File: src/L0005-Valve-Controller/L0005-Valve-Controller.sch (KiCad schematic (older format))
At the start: 24 parts, among them P1 3220-20-0200-00, U1 LPC54113J256BD64QL, U2 LMS8117AMP-3.3_NOPB

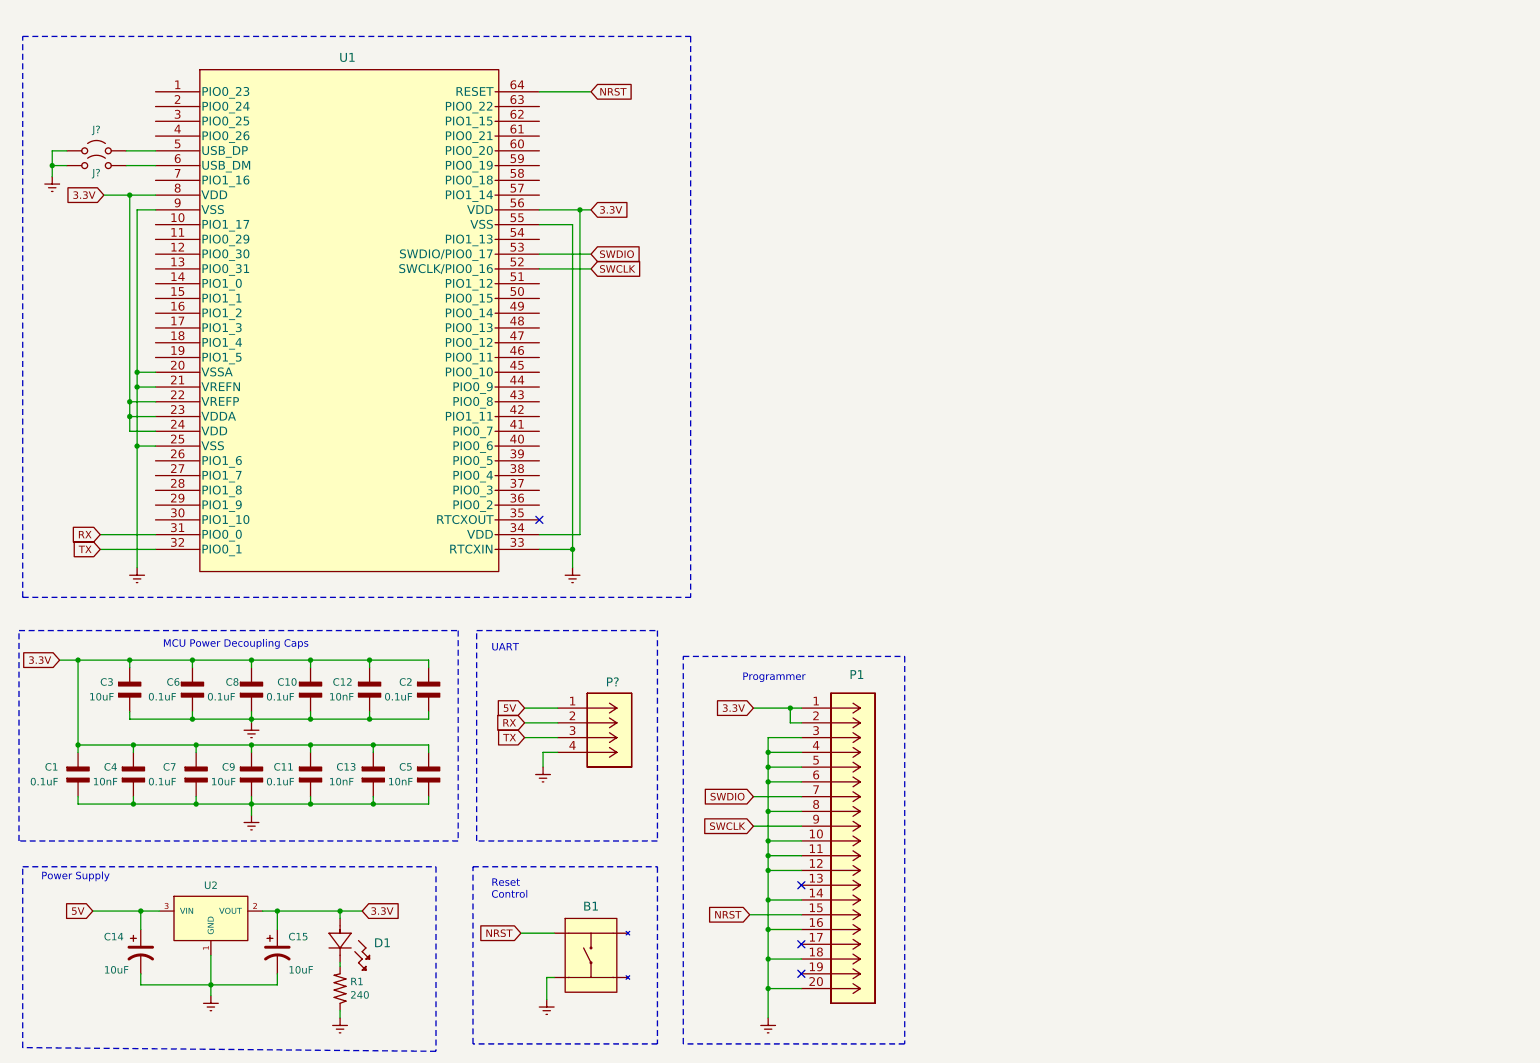
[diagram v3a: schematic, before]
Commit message: Added SSR Solenoid drivers to schematic
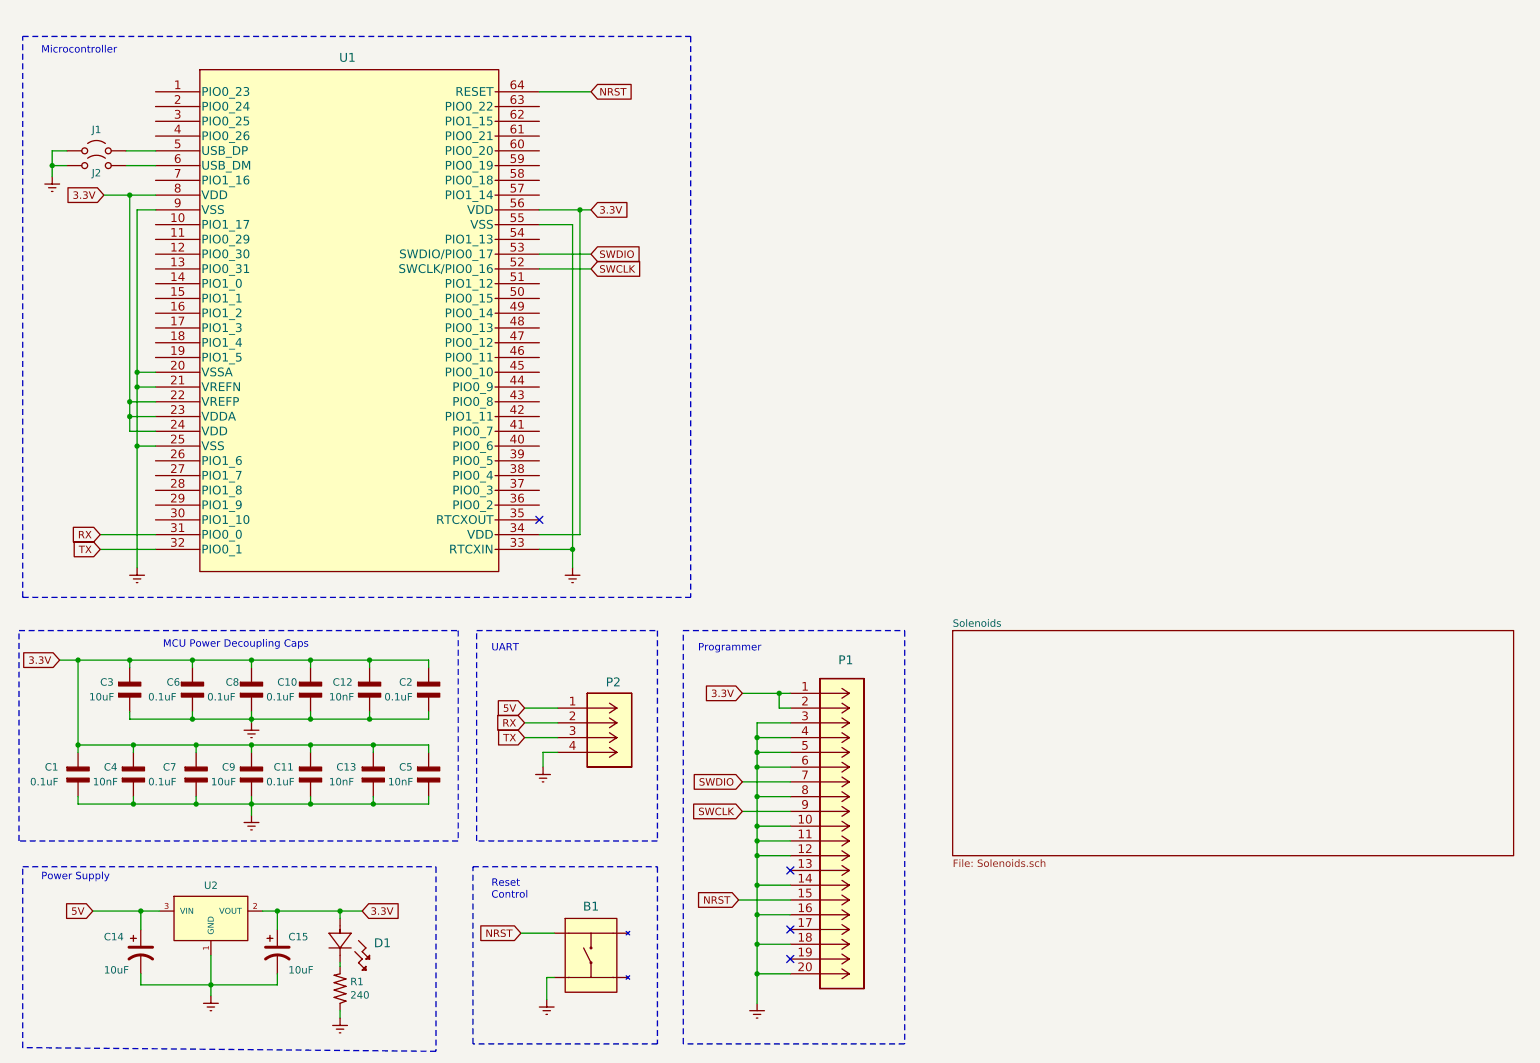
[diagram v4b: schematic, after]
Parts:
- gave numbers to parts that had none: 3
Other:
- note added: "Microcontroller"
- moved on the sheet: P1
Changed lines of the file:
@@
 $Descr A4 11693 8268
 encoding utf-8
-Sheet 1 1
+Sheet 1 2
 Title "L0005 Valve Controller"
 Date "2021-12-25"
@@
 $EndComp
 NoConn ~ 4300 4025
-Text Notes 5675 5125 0    50   ~ 0
+Text Notes 5375 4925 0    50   ~ 0
 Programmer
 $Comp
 L L0005-Valve-Controller:3220-20-0200-00 P1
 U 1 1 61D6852B
-P 6075 5300
-F 0 "P1" H 6400 5525 60  0000 L CNN
-F 1 "3220-20-0200-00" H 6475 5450 60  0001 C CNN
-F 2 "CONN20_D10-RA-BK_SUL" H 6475 4240 60  0001 C CNN
-F 3 "" H 6075 5300 60  0001 C CNN
-	1    6075 5300
-	1    0    0    -1
-$EndComp
-Text GLabel 5750 5300 0    50   Input ~ 0
+P 6000 5200
+F 0 "P1" H 6325 5425 60  0000 L CNN
+F 1 "3220-20-0200-00" H 6400 5350 60  0001 C CNN
+F 2 "CONN20_D10-RA-BK_SUL" H 6400 4140 60  0001 C CNN
+F 3 "" H 6000 5200 60  0001 C CNN
+	1    6000 5200
+	1    0    0    -1
+$EndComp
+Text GLabel 5675 5200 0    50   Input ~ 0
 3.3V
 Wire Wire Line
-	5750 5300 6000 5300
-Wire Wire Line
-	6075 5400 6000 5400
-Wire Wire Line
-	6000 5400 6000 5300
-Connection ~ 6000 5300
-Wire Wire Line
-	6000 5300 6075 5300
+	5675 5200 5925 5200
+Wire Wire Line
+	6000 5300 5925 5300
+Wire Wire Line
+	5925 5300 5925 5200
+Connection ~ 5925 5200
+Wire Wire Line
+	5925 5200 6000 5200
 $Comp
 L L0005-Valve-Controller:Earth #PWR08
 U 1 1 61D80BAC
-P 5850 7400
-F 0 "#PWR08" H 5850 7150 50  0001 C CNN
-F 1 "Earth" H 5850 7250 50  0001 C CNN
-F 2 "" H 5850 7400 50  0001 C CNN
-F 3 "" H 5850 7400 50  0001 C CNN
-	1    5850 7400
-	1    0    0    -1
-$EndComp
-Wire Wire Line
-	6075 5500 5850 5500
-Wire Wire Line
-	5850 5500 5850 5600
-Wire Wire Line
-	6075 5600 5850 5600
-Connection ~ 5850 5600
-Wire Wire Line
-	5850 5600 5850 5700
-Wire Wire Line
-	6075 5700 5850 5700
-Connection ~ 5850 5700
-Wire Wire Line
-	5850 5700 5850 5800
-Wire Wire Line
-	6075 5800 5850 5800
-Connection ~ 5850 5800
-Wire Wire Line
-	5850 5800 5850 6000
-Text GLabel 5750 5900 0    50   Input ~ 0
+P 5775 7300
+F 0 "#PWR08" H 5775 7050 50  0001 C CNN
+F 1 "Earth" H 5775 7150 50  0001 C CNN
+F 2 "" H 5775 7300 50  0001 C CNN
+F 3 "" H 5775 7300 50  0001 C CNN
+	1    5775 7300
+	1    0    0    -1
+$EndComp
+Wire Wire Line
+	6000 5400 5775 5400
+Wire Wire Line
+	5775 5400 5775 5500
+Wire Wire Line
+	6000 5500 5775 5500
+Connection ~ 5775 5500
+Wire Wire Line
+	5775 5500 5775 5600
+Wire Wire Line
+	6000 5600 5775 5600
+Connection ~ 5775 5600
+Wire Wire Line
+	5775 5600 5775 5700
+Wire Wire Line
+	6000 5700 5775 5700
+Connection ~ 5775 5700
+Wire Wire Line
+	5775 5700 5775 5900
+Text GLabel 5675 5800 0    50   Input ~ 0
 SWDIO
 Wire Wire Line
-	6075 5900 5750 5900
-Text GLabel 5750 6100 0    50   Input ~ 0
+	6000 5800 5675 5800
+Text GLabel 5675 6000 0    50   Input ~ 0
 SWCLK
 Wire Wire Line
-	6075 6100 5750 6100
-Wire Wire Line
-	6075 6000 5850 6000
-Connection ~ 5850 6000
-Wire Wire Line
-	5850 6000 5850 6200
-Wire Wire Line
-	6075 6200 5850 6200
-Connection ~ 5850 6200
-Wire Wire Line
-	6075 6400 5850 6400
-Connection ~ 5850 6400
-Wire Wire Line
-	5850 6200 5850 6300
-Wire Wire Line
-	5850 6400 5850 6600
-Wire Wire Line
-	6075 6600 5850 6600
-Connection ~ 5850 6600
-Wire Wire Line
-	5850 6600 5850 6800
-Wire Wire Line
-	6075 6800 5850 6800
-Connection ~ 5850 6800
-Wire Wire Line
-	5850 6800 5850 7000
-Wire Wire Line
-	6075 7000 5850 7000
-Connection ~ 5850 7000
-Wire Wire Line
-	5850 7000 5850 7200
-Wire Wire Line
-	6075 7200 5850 7200
-Connection ~ 5850 7200
-Wire Wire Line
-	5850 7200 5850 7400
-Text GLabel 5725 6700 0    50   Input ~ 0
+	6000 6000 5675 6000
+Wire Wire Line
+	6000 5900 5775 5900
+Connection ~ 5775 5900
+Wire Wire Line
+	5775 5900 5775 6100
+Wire Wire Line
+	6000 6100 5775 6100
+Connection ~ 5775 6100
+Wire Wire Line
+	6000 6300 5775 6300
+Connection ~ 5775 6300
+Wire Wire Line
+	5775 6100 5775 6200
+Wire Wire Line
+	5775 6300 5775 6500
+Wire Wire Line
+	6000 6500 5775 6500
+Connection ~ 5775 6500
+Wire Wire Line
+	5775 6500 5775 6700
+Wire Wire Line
+	6000 6700 5775 6700
+Connection ~ 5775 6700
+Wire Wire Line
+	5775 6700 5775 6900
+Wire Wire Line
+	6000 6900 5775 6900
+Connection ~ 5775 6900
+Wire Wire Line
+	5775 6900 5775 7100
+Wire Wire Line
+	6000 7100 5775 7100
+Connection ~ 5775 7100
+Wire Wire Line
+	5775 7100 5775 7300
+Text GLabel 5650 6600 0    50   Input ~ 0
 NRST
 Wire Wire Line
-	5725 6700 6075 6700
-Wire Wire Line
-	6075 6300 5850 6300
-Connection ~ 5850 6300
-Wire Wire Line
-	5850 6300 5850 6400
-NoConn ~ 6075 6500
-NoConn ~ 6075 7100
-NoConn ~ 6075 6900
+	5650 6600 6000 6600
+Wire Wire Line
+	6000 6200 5775 6200
+Connection ~ 5775 6200
+Wire Wire Line
+	5775 6200 5775 6300
+NoConn ~ 6000 6400
+NoConn ~ 6000 7000
+NoConn ~ 6000 6800
 Text GLabel 4650 2225 2    50   Input ~ 0
 SWDIO
@@
 	4650 2325 4300 2325
 Wire Notes Line
-	5275 4950 6775 4950
-Wire Notes Line
-	6775 4950 6775 7575
+	5275 4775 6775 4775
+Wire Notes Line
+	6775 4775 6775 7575
 Wire Notes Line
 	6775 7575 5275 7575
 Wire Notes Line
-	5275 7575 5275 4950
+	5275 7575 5275 4775
 Wire Notes Line
 	3750 6200 775  6200
@@
 Reset \nControl
 $Comp
-L L0005-Valve-Controller:Jumper_NO J?
+L L0005-Valve-Controller:Jumper_NO J1
 U 1 1 620B41A7
 P 1300 1525
-F 0 "J?" H 1300 1668 50  0000 C CNN
+F 0 "J1" H 1300 1668 50  0000 C CNN
 F 1 "Jumper_NO" H 1300 1435 50  0001 C CNN
 F 2 "" H 1300 1525 50  0001 C CNN
@@
 $EndComp
 $Comp
-L L0005-Valve-Controller:Jumper_NO J?
+L L0005-Valve-Controller:Jumper_NO J2
 U 1 1 620C12B9
 P 1300 1625
-F 0 "J?" H 1300 1575 50  0000 C CNN
+F 0 "J2" H 1300 1575 50  0000 C CNN
 F 1 "Jumper_NO" H 1300 1535 50  0001 C CNN
 F 2 "" H 1300 1625 50  0001 C CNN
@@
 	1500 1625 1700 1625
 $Comp
-L L0005-Valve-Controller:Earth #PWR?
+L L0005-Valve-Controller:Earth #PWR09
 U 1 1 620CE508
 P 1000 1700
-F 0 "#PWR?" H 1000 1450 50  0001 C CNN
+F 0 "#PWR09" H 1000 1450 50  0001 C CNN
 F 1 "Earth" H 1000 1550 50  0001 C CNN
 F 2 "" H 1000 1700 50  0001 C CNN
@@
 	775  4775 3750 4775
 $Comp
-L L0005-Valve-Controller:140-504-415-000 P?
+L L0005-Valve-Controller:140-504-415-000 P2
 U 1 1 622DBA6B
 P 4425 5300
-F 0 "P?" H 4750 5475 60  0000 L CNN
+F 0 "P2" H 4750 5475 60  0000 L CNN
 F 1 "140-504-415-000" H 4775 4850 60  0001 C CNN
 F 2 "CONN_4840.2201_SCH" H 4825 4700 60  0001 C CNN
@@
 	4200 5300 4425 5300
 $Comp
-L L0005-Valve-Controller:Earth #PWR?
+L L0005-Valve-Controller:Earth #PWR010
 U 1 1 622F0D80
 P 4325 5700
-F 0 "#PWR?" H 4325 5450 50  0001 C CNN
+F 0 "#PWR010" H 4325 5450 50  0001 C CNN
 F 1 "Earth" H 4325 5550 50  0001 C CNN
 F 2 "" H 4325 5700 50  0001 C CNN
@@
 Wire Wire Line
 	1700 4225 1325 4225
+Text Notes 925  875  0    50   ~ 0
+Microcontroller
+$Sheet
+S 7100 4775 3800 1525
+U 624AA92C
+F0 "Solenoids" 50
+F1 "Solenoids.sch" 50
+$EndSheet
 $EndSCHEMATC

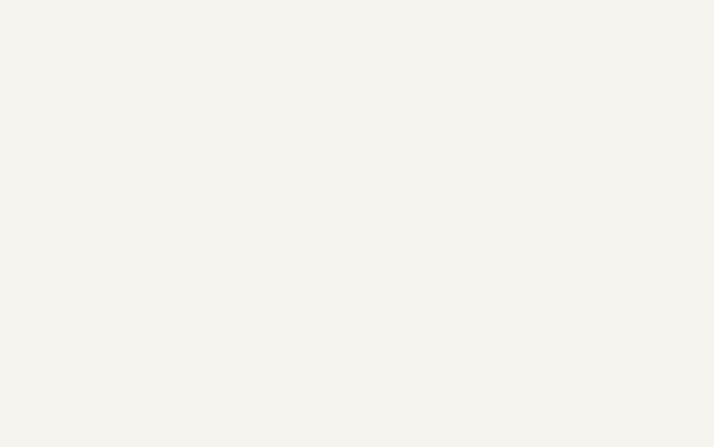
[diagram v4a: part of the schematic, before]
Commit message: Added AC source to schematic
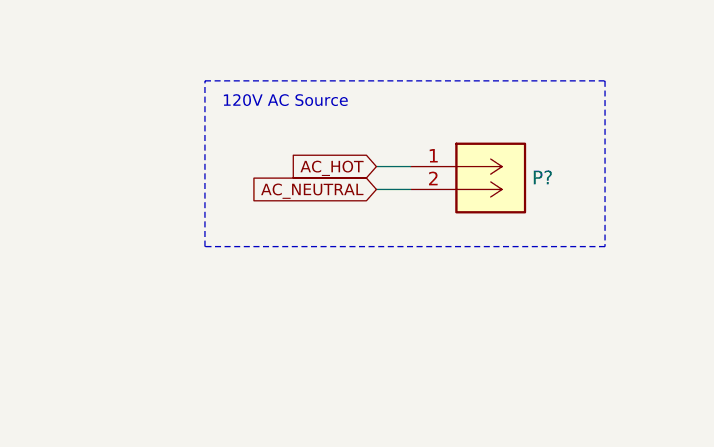
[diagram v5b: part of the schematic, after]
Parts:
- added P?: 647676-2, CONN_2043-1X04G00DAU_OUP, symbol L0005-Valve-Controller:647676-2
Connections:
- new net AC_HOT: P?.1
- new net AC_NEUTRAL: P?.2
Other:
- note added: "120V AC Source"
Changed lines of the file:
@@
 F1 "Solenoids.sch" 50
 $EndSheet
+$Comp
+L L0005-Valve-Controller:647676-2 P?
+U 1 1 62660979
+P 9650 1400
+F 0 "P?" H 10180 1350 60  0000 L CNN
+F 1 "647676-2" H 10178 1297 60  0001 L CNN
+F 2 "CONN_2043-1X04G00DAU_OUP" H 10000 850 60  0001 C CNN
+F 3 "" H 9650 1400 60  0001 C CNN
+	1    9650 1400
+	1    0    0    -1
+$EndComp
+Text GLabel 9500 1400 0    50   Input ~ 0
+AC_HOT
+Wire Wire Line
+	9500 1400 9650 1400
+Text GLabel 9500 1500 0    50   Input ~ 0
+AC_NEUTRAL
+Wire Wire Line
+	9500 1500 9650 1500
+Wire Notes Line
+	8750 1025 10500 1025
+Wire Notes Line
+	10500 1025 10500 1750
+Wire Notes Line
+	10500 1750 8750 1750
+Wire Notes Line
+	8750 1750 8750 1025
+Text Notes 8825 1150 0    50   ~ 0
+120V AC Source
 $EndSCHEMATC
